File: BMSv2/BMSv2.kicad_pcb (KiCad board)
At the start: 2 copper layers, 44 x 41.2 mm, 126 parts, among them J1 Conn_01x05, J2 Conn_01x04_Socket, J3 Conn_01x02_Pin, J4 Conn_01x02_Pin, J5 Conn_01x03_Pin, Q1 AO3401A, Q10 MMBT3904, Q11 MMBT3904, Q12 MMBT3904, Q13 MMBT3904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

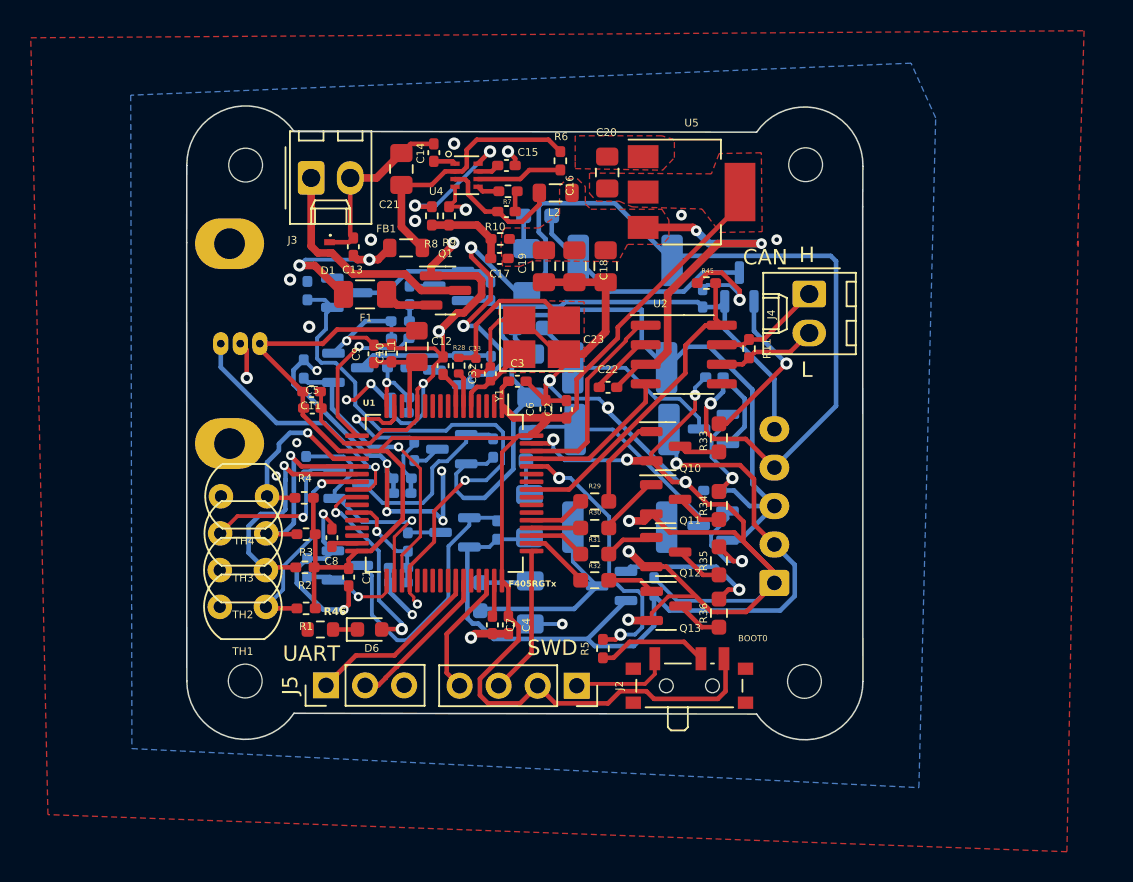
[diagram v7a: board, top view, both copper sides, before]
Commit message: added BOM and changed Vias
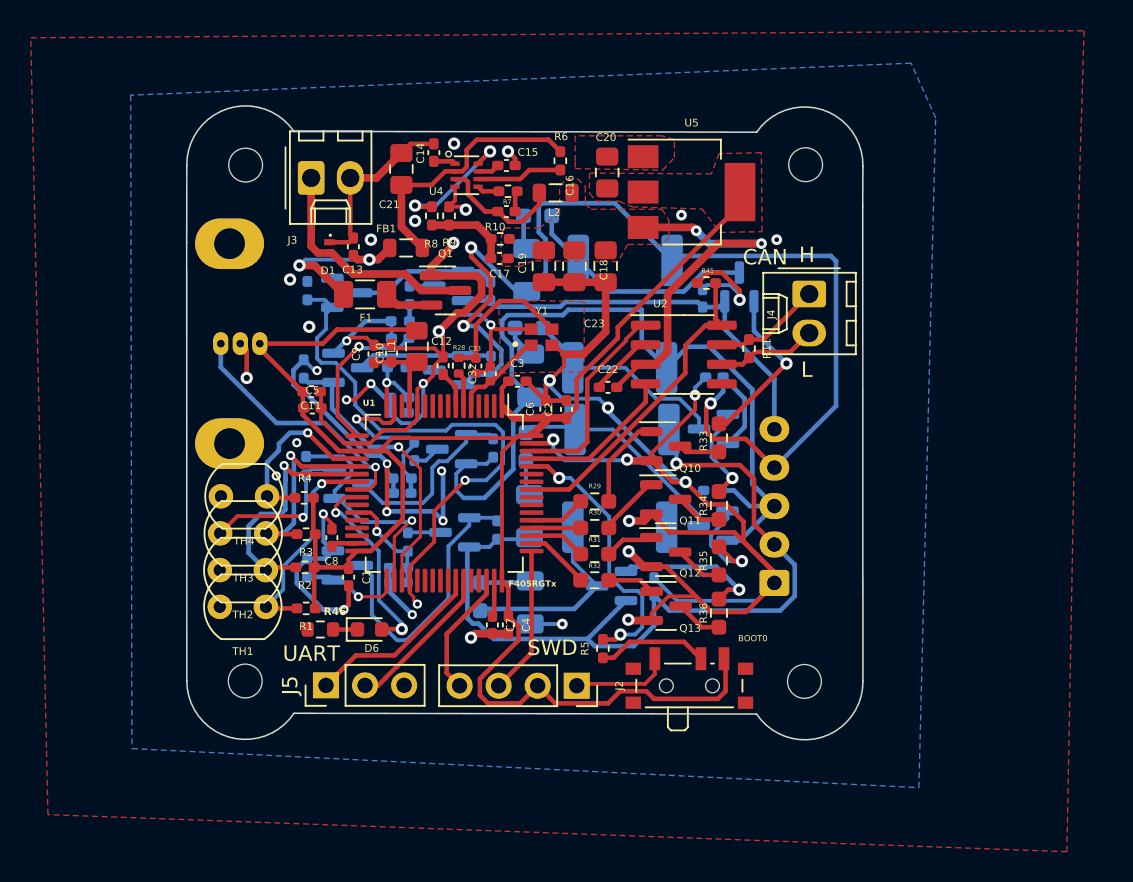
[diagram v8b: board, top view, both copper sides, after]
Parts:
- Y1: footprint footprints:Kryształ_16MHz_BMS -> footprints:XTAL_ECS-160-10-37-JTN-TR
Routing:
- net +3.3V: track 120.2 -> 118.2 mm
- net +5V: track 24.0 -> 22.6 mm
- net Net-(Q14-C): track 16.6 -> 15.4 mm
- net CELL3: track 75.6 -> 74.5 mm
- net CELL1: track 54.3 -> 53.3 mm
- net HSE_IN: track 5.04 -> 5.94 mm
- net CAN1_TX: track 13.7 -> 12.9 mm
- net Net-(Q11-B): track 4.49 -> 3.70 mm
- net Net-(Q15-C): track 13.7 -> 13.0 mm
- net Net-(C33-Pad1): track 10.2 -> 9.60 mm
- net CELL1_M_TRIG: track 6.57 -> 6.01 mm
- net GND: track 246.5 -> 246.4 mm, vias 39 -> 40
